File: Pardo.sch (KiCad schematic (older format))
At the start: 36 parts, among them J1 USB_OTG, J2 Conn_02x01, J3 Conn_02x01, J4 Conn_02x01, J5 Conn_02x01, J7 Conn_02x01, SW1 SW_Push, U1 ATSAMD21G18A-AUT, U2 TPS73733DCQR, U3 MCP73832T-2ACI_OT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

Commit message: minor updates
Signed-off-by: Ricardo Mena C <rgacort12@gmail.com>
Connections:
- no-connect marks 0 -> 1
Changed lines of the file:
@@
 Text Notes 6775 2100 0    47   ~ 0
 User \nLED
+NoConn ~ 4075 2200
 $EndSCHEMATC

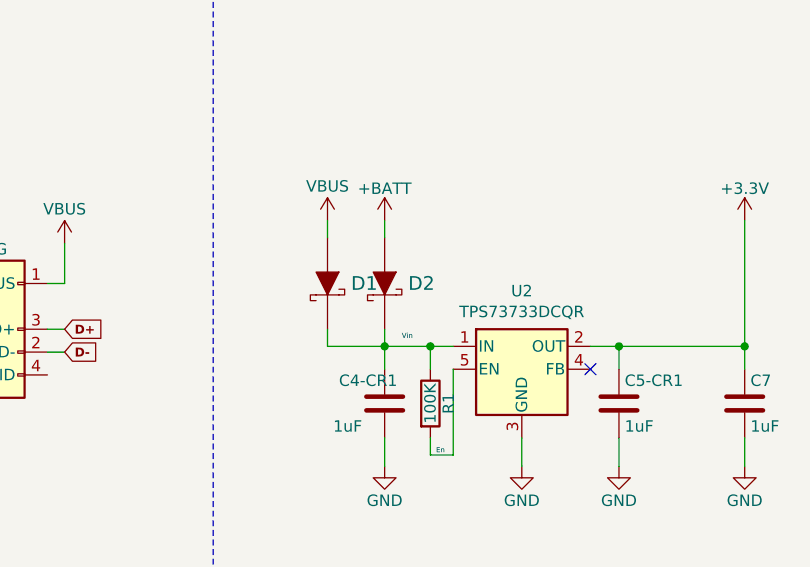
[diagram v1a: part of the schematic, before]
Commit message: D2 batt schk deleted
Signed-off-by: Ricardo Mena C <rgacort12@gmail.com>
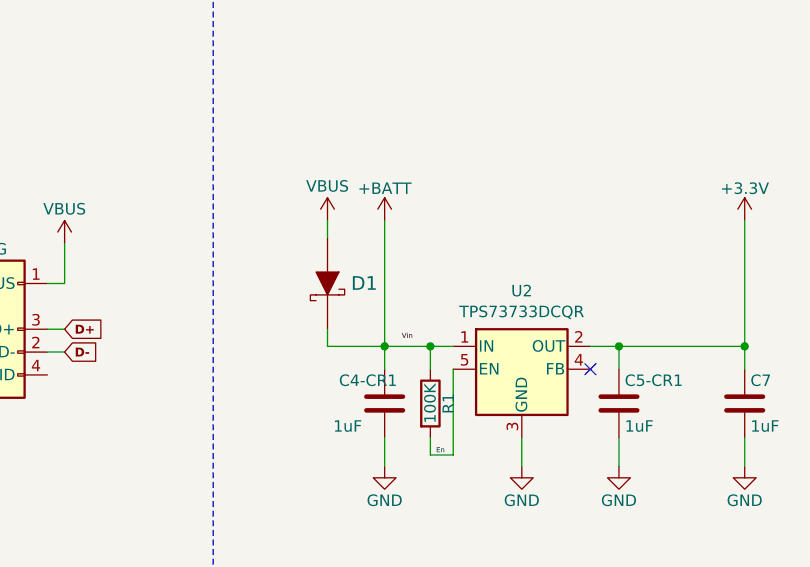
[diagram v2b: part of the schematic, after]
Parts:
- removed D2: MBR0520LT1G, digikey-footprints:SOD-123, symbol Pardo-rescue:MBR0520LT1G-dk_Diodes-Rectifiers-Single
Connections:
- net +BATT: now also C4-CR1.1, D1.K, R1.1, U2.1 (IN)
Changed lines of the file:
@@
 	0    1    1    0
 $EndComp
-$Comp
-L Pardo-rescue:MBR0520LT1G-dk_Diodes-Rectifiers-Single D2
-U 1 1 5E9E757D
-P 3175 1825
-F 0 "D2" V 3175 1928 60  0000 L CNN
-F 1 "MBR0520LT1G" V 3228 1928 60  0001 L CNN
-F 2 "digikey-footprints:SOD-123" H 3375 2025 60  0001 L CNN
-F 3 "http://www.onsemi.com/pub/Collateral/MBR0520LT1-D.PDF" H 3375 2125 60  0001 L CNN
-F 4 "MBR0520LT1GOSCT-ND" H 3375 2225 60  0001 L CNN "Digi-Key_PN"
-F 5 "MBR0520LT1G" H 3375 2325 60  0001 L CNN "MPN"
-F 6 "Discrete Semiconductor Products" H 3375 2425 60  0001 L CNN "Category"
-F 7 "Diodes - Rectifiers - Single" H 3375 2525 60  0001 L CNN "Family"
-F 8 "http://www.onsemi.com/pub/Collateral/MBR0520LT1-D.PDF" H 3375 2625 60  0001 L CNN "DK_Datasheet_Link"
-F 9 "/product-detail/en/on-semiconductor/MBR0520LT1G/MBR0520LT1GOSCT-ND/917965" H 3375 2725 60  0001 L CNN "DK_Detail_Page"
-F 10 "DIODE SCHOTTKY 20V 500MA SOD123" H 3375 2825 60  0001 L CNN "Description"
-F 11 "ON Semiconductor" H 3375 2925 60  0001 L CNN "Manufacturer"
-F 12 "Active" H 3375 3025 60  0001 L CNN "Status"
-	1    3175 1825
-	0    1    1    0
-$EndComp
 Wire Wire Line
 	2925 1550 2925 1625
 Wire Wire Line
-	3175 1550 3175 1625
-Wire Wire Line
 	2925 2025 2925 2100
-Wire Wire Line
-	3175 2025 3175 2100
 $Comp
 L Custom_lib:TPS73733DCQR U2
@@
 User \nLED
 NoConn ~ 4075 2200
+Wire Wire Line
+	3175 1550 3175 2100
 $EndSCHEMATC

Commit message: D2 batt schk restore
Signed-off-by: Ricardo Mena C <rgacort12@gmail.com>
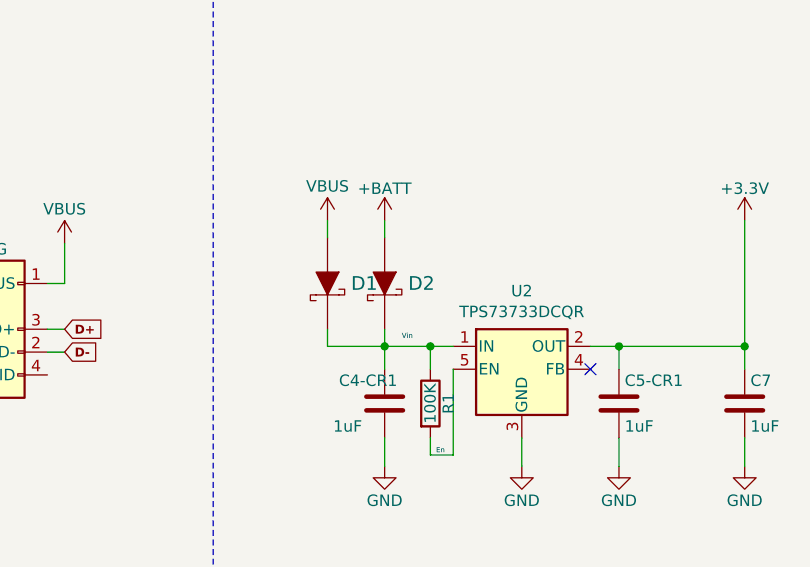
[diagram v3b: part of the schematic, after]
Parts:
- added D2: MBR0520LT1G, digikey-footprints:SOD-123, symbol Pardo-rescue:MBR0520LT1G-dk_Diodes-Rectifiers-Single
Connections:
- net +BATT: now also D2.A; no longer C4-CR1.1, D1.K, R1.1, U2.1 (IN)
- new net: C4-CR1.1, D1.K, D2.K, R1.1, U2.1 (IN)
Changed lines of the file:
@@
 NoConn ~ 4075 2200
 Wire Wire Line
-	3175 1550 3175 2100
+	3175 2025 3175 2100
+Wire Wire Line
+	3175 1550 3175 1625
+$Comp
+L Pardo-rescue:MBR0520LT1G-dk_Diodes-Rectifiers-Single D2
+U 1 1 5E9E757D
+P 3175 1825
+F 0 "D2" V 3175 1928 60  0000 L CNN
+F 1 "MBR0520LT1G" V 3228 1928 60  0001 L CNN
+F 2 "digikey-footprints:SOD-123" H 3375 2025 60  0001 L CNN
+F 3 "http://www.onsemi.com/pub/Collateral/MBR0520LT1-D.PDF" H 3375 2125 60  0001 L CNN
+F 4 "MBR0520LT1GOSCT-ND" H 3375 2225 60  0001 L CNN "Digi-Key_PN"
+F 5 "MBR0520LT1G" H 3375 2325 60  0001 L CNN "MPN"
+F 6 "Discrete Semiconductor Products" H 3375 2425 60  0001 L CNN "Category"
+F 7 "Diodes - Rectifiers - Single" H 3375 2525 60  0001 L CNN "Family"
+F 8 "http://www.onsemi.com/pub/Collateral/MBR0520LT1-D.PDF" H 3375 2625 60  0001 L CNN "DK_Datasheet_Link"
+F 9 "/product-detail/en/on-semiconductor/MBR0520LT1G/MBR0520LT1GOSCT-ND/917965" H 3375 2725 60  0001 L CNN "DK_Detail_Page"
+F 10 "DIODE SCHOTTKY 20V 500MA SOD123" H 3375 2825 60  0001 L CNN "Description"
+F 11 "ON Semiconductor" H 3375 2925 60  0001 L CNN "Manufacturer"
+F 12 "Active" H 3375 3025 60  0001 L CNN "Status"
+	1    3175 1825
+	0    1    1    0
+$EndComp
 $EndSCHEMATC
